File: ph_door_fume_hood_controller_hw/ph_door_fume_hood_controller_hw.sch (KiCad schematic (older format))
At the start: 249 parts, among them IC1 6N137, IC2 6N137, J1 Conn_01x03, J10 Conn_01x03, J11 Conn_01x02, J12 Conn_01x06, J13 Conn_01x02, J14 Conn_01x03, J15 Conn_01x03, J2 Conn_01x04, J3 CONN_01X04, J4 Conn_01x03, J5 Conn_01x03, J6 Conn_01x02, J7 Conn_01x06, J8 USB_OTG, J9 Conn_01x02, M1 DC-DC-24-12V-200mA, M2 MORSUN_485, Q1 C1815, Q10 A1015, Q11 Q_NMOS_GDS, Q2 Q_PMOS_GDS, Q3 Q_NMOS_GDS, Q4 Q_NMOS_GDS, Q5 C1815, Q6 Q_NMOS_GDS, Q7 Q_NMOS_GDS, Q8 C1815, Q9 Q_NMOS_GDS, U1 74HC123, U10 PC817, U11 MCP4725, U12 ASM1117-3V3, U13 PC817, U14 PC817, U15 LM358, U16 PC817, U17 PC817, U18 PC817, U19 PC817, U2 AD8601, U20 PC817, U21 PC817, U22 PC817, U23 PC817, U3 PC817, U4 PC817, U5 TB6600, U6 PC817, U7 STM32F103C8, U8 ASM1117, U9 XL4015, Y1 Crystal, Y2 32768Mhz

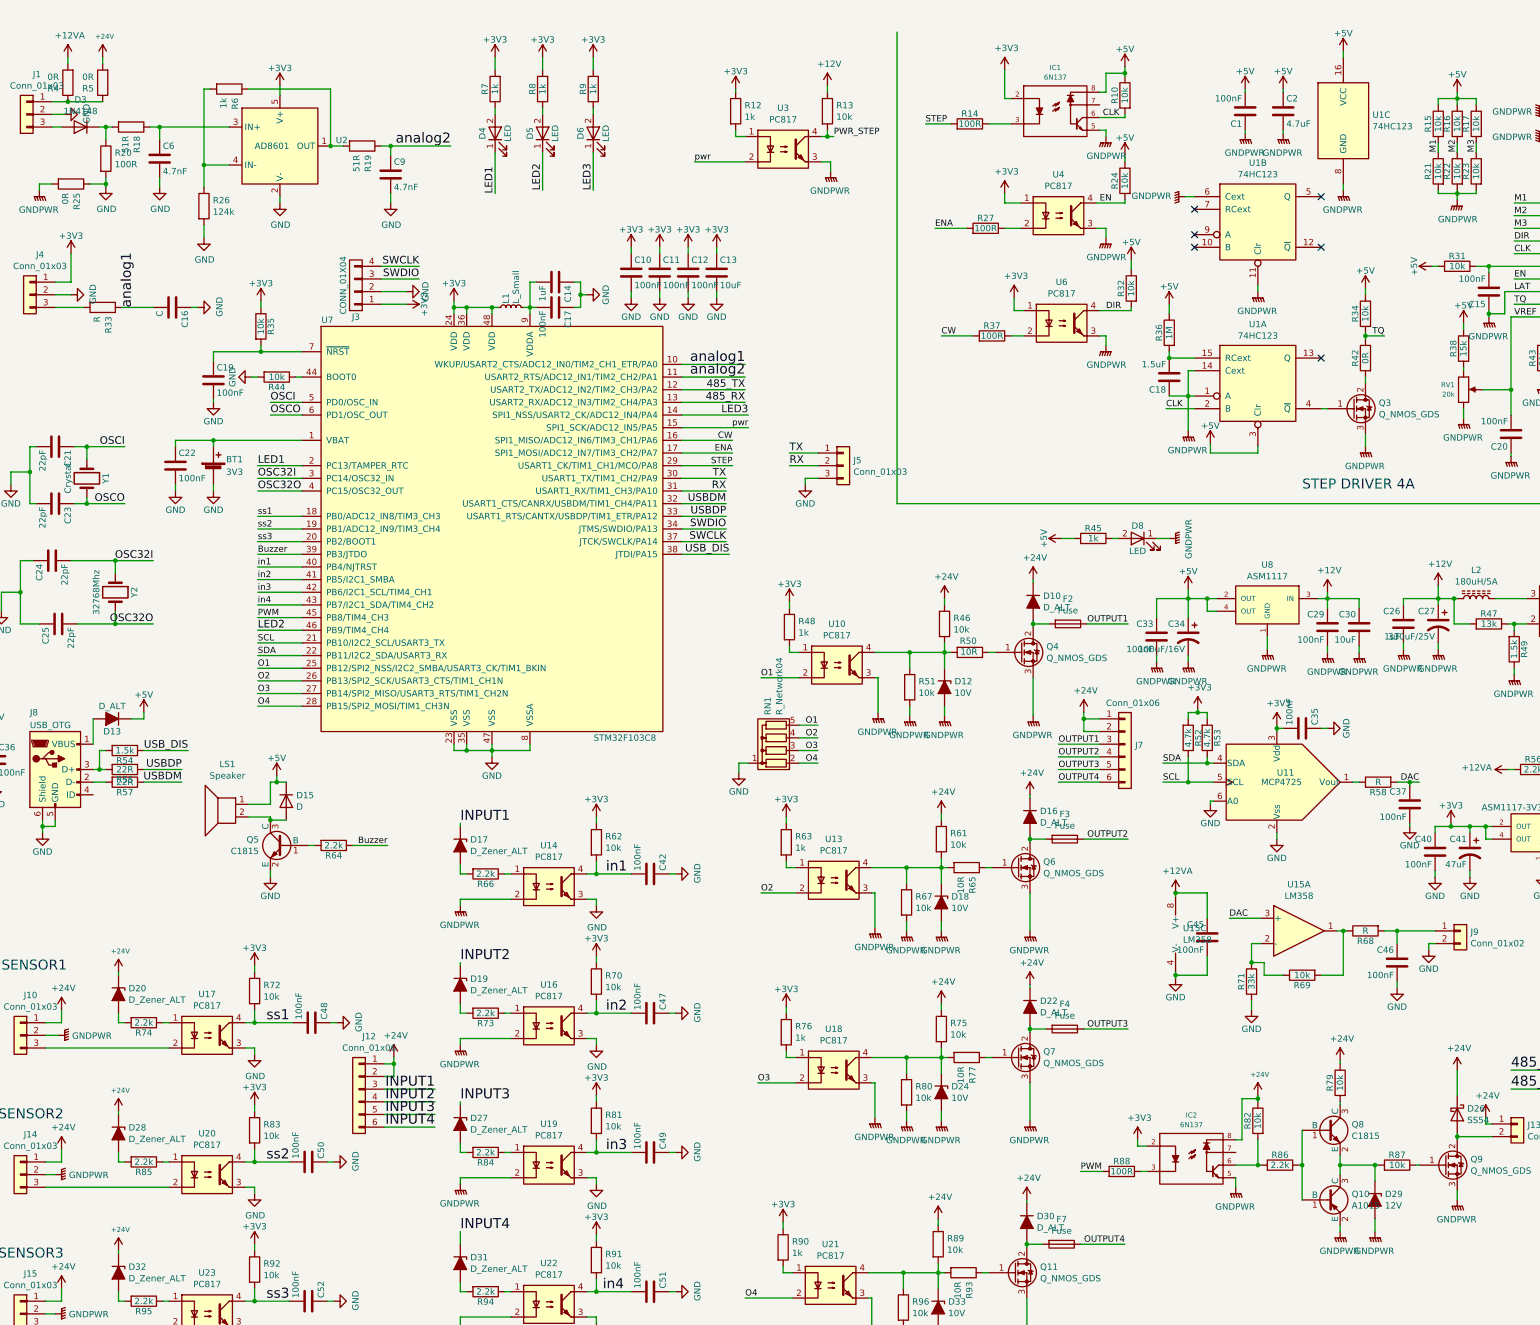
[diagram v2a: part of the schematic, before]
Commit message: Layoutting Board Door-Fume-Hood
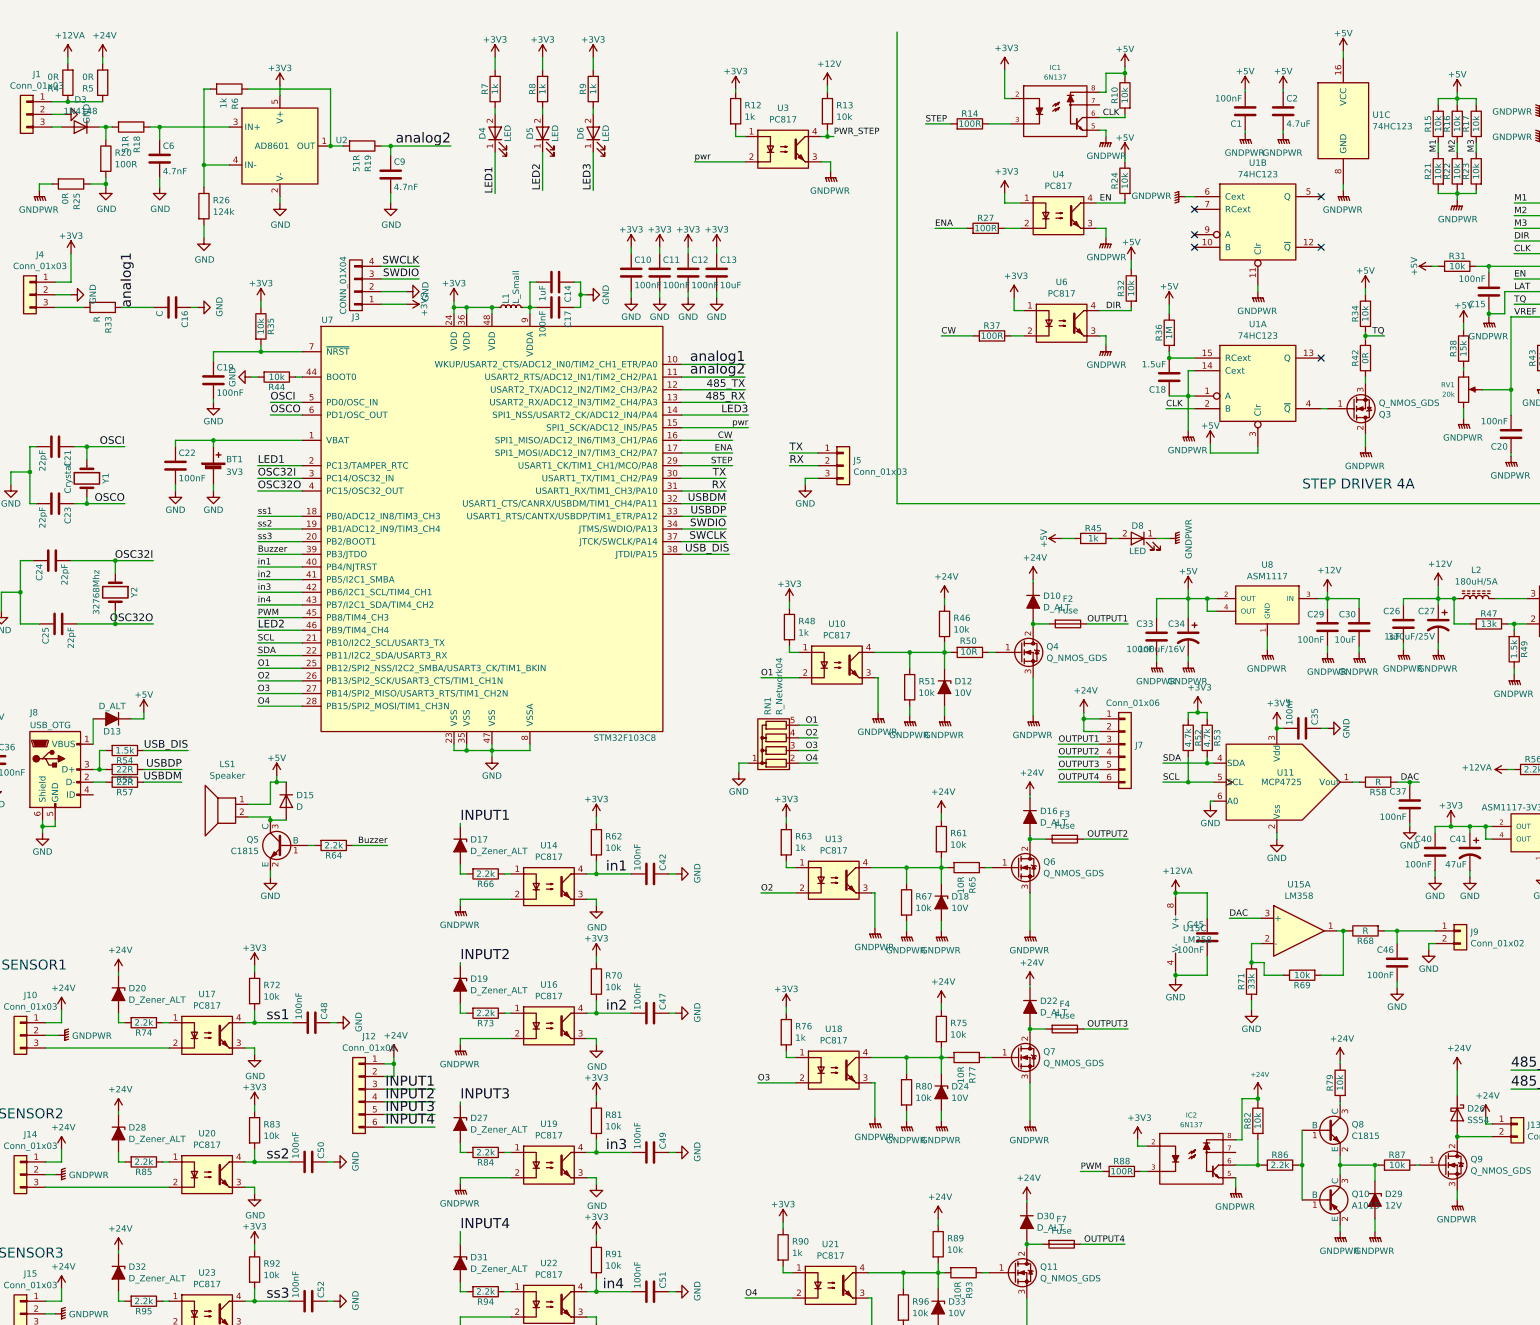
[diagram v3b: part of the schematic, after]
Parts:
- J1, J4, J5: footprint VinhTho_Lib:TerminalBlock-WAGO-3P -> Connector_PinSocket_2.54mm:PinSocket_1x03_P2.54mm_Vertical
- J10, J14, J15: footprint VinhTho_Lib:TerminalBlock-WAGO-3P -> VinhTho_Lib:TerminalBlock_WAGO_2.54mm_3P
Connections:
- net +24V: now also D20.1 (K), D28.1 (K), D32.1 (K), R5.2
- net GNDPWR: now also Q3.2 (D); no longer Q3.3 (S)
- net at R42.2: now also Q3.3 (S); no longer Q3.2 (D)
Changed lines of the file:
@@
 $EndComp
 $Comp
-L master-node-rescue:C C10
-U 1 1 595ADDFC
-P 5550 2400
-F 0 "C10" H 5575 2500 50  0000 L CNN
-F 1 "100nF" H 5575 2300 50  0000 L CNN
-F 2 "Capacitor_SMD:C_0805_2012Metric_Pad1.15x1.40mm_HandSolder" H 5588 2250 50  0001 C CNN
-F 3 "" H 5550 2400 50  0001 C CNN
-	1    5550 2400
-	1    0    0    -1
-$EndComp
-$Comp
 L master-node-rescue:+3V3 #PWR063
 U 1 1 595B16DC
@@
 F 3 "https://banlinhkien.com/30n06-fqd30n06-to252-mosfet-nch-22a-60v-p12118703.html" H 11250 3475 50  0001 C CNN
 	1    11250 3475
-	1    0    0    -1
+	1    0    0    1
 $EndComp
 Wire Wire Line
@@
 $EndComp
 $Comp
-L ph_door_fume_hood_controller_hw-rescue:+24V-PH_LIB #PWR0153
-U 1 1 5ED636E7
-P 1500 7925
-F 0 "#PWR0153" H 1500 7775 50  0001 C CNN
-F 1 "+24V" H 1515 8090 39  0000 C CNN
-F 2 "" H 1500 7925 50  0001 C CNN
-F 3 "" H 1500 7925 50  0001 C CNN
-	1    1500 7925
-	1    0    0    -1
-$EndComp
-$Comp
 L Device:D_Zener_ALT D20
 U 1 1 5ED63ED3
@@
 $EndComp
 $Comp
-L ph_door_fume_hood_controller_hw-rescue:+24V-PH_LIB #PWR0175
-U 1 1 5EEE7342
-P 1500 9025
-F 0 "#PWR0175" H 1500 8875 50  0001 C CNN
-F 1 "+24V" H 1515 9190 39  0000 C CNN
-F 2 "" H 1500 9025 50  0001 C CNN
-F 3 "" H 1500 9025 50  0001 C CNN
-	1    1500 9025
-	1    0    0    -1
-$EndComp
-$Comp
 L Device:D_Zener_ALT D28
 U 1 1 5EEE7348
@@
 	2575 9425 2850 9425
 $Comp
-L Isolator:PC817 U23
-U 1 1 5EF16235
-P 2200 10625
-F 0 "U23" H 2200 10950 50  0000 C CNN
-F 1 "PC817" H 2200 10859 50  0000 C CNN
-F 2 "Package_DIP:DIP-4_W7.62mm" H 2000 10425 50  0001 L CIN
-F 3 "http://www.soselectronic.cz/a_info/resource/d/pc817.pdf" H 2200 10625 50  0001 L CNN
-	1    2200 10625
-	1    0    0    -1
-$EndComp
-$Comp
-L ph_door_fume_hood_controller_hw-rescue:+24V-PH_LIB #PWR0198
-U 1 1 5EF1623B
-P 1500 10125
-F 0 "#PWR0198" H 1500 9975 50  0001 C CNN
-F 1 "+24V" H 1515 10290 39  0000 C CNN
-F 2 "" H 1500 10125 50  0001 C CNN
-F 3 "" H 1500 10125 50  0001 C CNN
-	1    1500 10125
-	1    0    0    -1
-$EndComp
-$Comp
 L Device:D_Zener_ALT D32
 U 1 1 5EF16241
@@
 F 0 "J4" H 720 2892 50  0000 C CNN
 F 1 "Conn_01x03" H 720 2801 50  0000 C CNN
-F 2 "VinhTho_Lib:TerminalBlock-WAGO-3P" H 800 2575 50  0001 C CNN
+F 2 "Connector_PinSocket_2.54mm:PinSocket_1x03_P2.54mm_Vertical" H 800 2575 50  0001 C CNN
 F 3 "~" H 800 2575 50  0001 C CNN
 	1    800  2575
@@
 F 0 "J10" H 645 8742 50  0000 C CNN
 F 1 "Conn_01x03" H 645 8651 50  0000 C CNN
-F 2 "VinhTho_Lib:TerminalBlock-WAGO-3P" H 725 8425 50  0001 C CNN
+F 2 "VinhTho_Lib:TerminalBlock_WAGO_2.54mm_3P" H 725 8425 50  0001 C CNN
 F 3 "~" H 725 8425 50  0001 C CNN
 	1    725  8425
@@
 F 0 "J14" H 645 9842 50  0000 C CNN
 F 1 "Conn_01x03" H 645 9751 50  0000 C CNN
-F 2 "VinhTho_Lib:TerminalBlock-WAGO-3P" H 725 9525 50  0001 C CNN
+F 2 "VinhTho_Lib:TerminalBlock_WAGO_2.54mm_3P" H 725 9525 50  0001 C CNN
 F 3 "~" H 725 9525 50  0001 C CNN
 	1    725  9525
@@
 F 0 "J15" H 645 10942 50  0000 C CNN
 F 1 "Conn_01x03" H 645 10851 50  0000 C CNN
-F 2 "VinhTho_Lib:TerminalBlock-WAGO-3P" H 725 10625 50  0001 C CNN
+F 2 "VinhTho_Lib:TerminalBlock_WAGO_2.54mm_3P" H 725 10625 50  0001 C CNN
 F 3 "~" H 725 10625 50  0001 C CNN
 	1    725  10625
@@
 F 0 "J1" H 695 1467 50  0000 C CNN
 F 1 "Conn_01x03" H 695 1376 50  0000 C CNN
-F 2 "VinhTho_Lib:TerminalBlock-WAGO-3P" H 775 1150 50  0001 C CNN
+F 2 "Connector_PinSocket_2.54mm:PinSocket_1x03_P2.54mm_Vertical" H 775 1150 50  0001 C CNN
 F 3 "~" H 775 1150 50  0001 C CNN
 	1    775  1150
@@
 Wire Wire Line
 	1100 700  1100 750
-$Comp
-L ph_door_fume_hood_controller_hw-rescue:+24V-PH_LIB #PWR04
-U 1 1 5DEE7A26
-P 1375 700
-F 0 "#PWR04" H 1375 550 50  0001 C CNN
-F 1 "+24V" H 1390 865 39  0000 C CNN
-F 2 "" H 1375 700 50  0001 C CNN
-F 3 "" H 1375 700 50  0001 C CNN
-	1    1375 700
-	1    0    0    -1
-$EndComp
 Wire Wire Line
 	5950 3525 6475 3525
@@
 F 0 "J5" H 7305 3967 50  0000 L CNN
 F 1 "Conn_01x03" H 7305 3876 50  0000 L CNN
-F 2 "VinhTho_Lib:TerminalBlock-WAGO-3P" H 7225 3925 50  0001 C CNN
+F 2 "Connector_PinSocket_2.54mm:PinSocket_1x03_P2.54mm_Vertical" H 7225 3925 50  0001 C CNN
 F 3 "~" H 7225 3925 50  0001 C CNN
 	1    7225 3925
@@
 $EndComp
 $Comp
-L power:+24V #PWR0134
-U 1 1 5E2D94A6
-P 15450 7000
-F 0 "#PWR0134" H 15450 6850 50  0001 C CNN
-F 1 "+24V" H 15465 7173 50  0000 C CNN
-F 2 "" H 15450 7000 50  0001 C CNN
-F 3 "" H 15450 7000 50  0001 C CNN
-	1    15450 7000
-	1    0    0    -1
-$EndComp
-$Comp
 L power:+24V #PWR0171
 U 1 1 5E2FE88F
@@
 $EndComp
 $Comp
-L power:+24V #PWR?
+L power:+24V #PWR0153
 U 1 1 5E724D4F
 P 1050 8225
-F 0 "#PWR?" H 1050 8075 50  0001 C CNN
+F 0 "#PWR0153" H 1050 8075 50  0001 C CNN
 F 1 "+24V" H 1065 8398 50  0000 C CNN
 F 2 "" H 1050 8225 50  0001 C CNN
@@
 $EndComp
 $Comp
-L power:+24V #PWR?
+L power:+24V #PWR0159
 U 1 1 5E725FB4
 P 1050 9325
-F 0 "#PWR?" H 1050 9175 50  0001 C CNN
+F 0 "#PWR0159" H 1050 9175 50  0001 C CNN
 F 1 "+24V" H 1065 9498 50  0000 C CNN
 F 2 "" H 1050 9325 50  0001 C CNN
@@
 $EndComp
 $Comp
-L power:+24V #PWR?
+L power:+24V #PWR0175
 U 1 1 5E7283B8
 P 1050 10425
-F 0 "#PWR?" H 1050 10275 50  0001 C CNN
+F 0 "#PWR0175" H 1050 10275 50  0001 C CNN
 F 1 "+24V" H 1065 10598 50  0000 C CNN
 F 2 "" H 1050 10425 50  0001 C CNN
@@
 	1    0    0    -1
 $EndComp
+$Comp
+L Isolator:PC817 U23
+U 1 1 5EF16235
+P 2200 10625
+F 0 "U23" H 2200 10950 50  0000 C CNN
+F 1 "PC817" H 2200 10859 50  0000 C CNN
+F 2 "Package_DIP:DIP-4_W7.62mm" H 2000 10425 50  0001 L CIN
+F 3 "http://www.soselectronic.cz/a_info/resource/d/pc817.pdf" H 2200 10625 50  0001 L CNN
+	1    2200 10625
+	1    0    0    -1
+$EndComp
+$Comp
+L power:+24V #PWR0182
+U 1 1 5DBF911F
+P 1500 7925
+F 0 "#PWR0182" H 1500 7775 50  0001 C CNN
+F 1 "+24V" H 1515 8098 50  0000 C CNN
+F 2 "" H 1500 7925 50  0001 C CNN
+F 3 "" H 1500 7925 50  0001 C CNN
+	1    1500 7925
+	1    0    0    -1
+$EndComp
+$Comp
+L power:+24V #PWR0198
+U 1 1 5DBF9B7E
+P 1500 9025
+F 0 "#PWR0198" H 1500 8875 50  0001 C CNN
+F 1 "+24V" H 1515 9198 50  0000 C CNN
+F 2 "" H 1500 9025 50  0001 C CNN
+F 3 "" H 1500 9025 50  0001 C CNN
+	1    1500 9025
+	1    0    0    -1
+$EndComp
+$Comp
+L power:+24V #PWR0199
+U 1 1 5DBFBF1F
+P 1500 10125
+F 0 "#PWR0199" H 1500 9975 50  0001 C CNN
+F 1 "+24V" H 1515 10298 50  0000 C CNN
+F 2 "" H 1500 10125 50  0001 C CNN
+F 3 "" H 1500 10125 50  0001 C CNN
+	1    1500 10125
+	1    0    0    -1
+$EndComp
+$Comp
+L power:+24V #PWR0213
+U 1 1 5DC75FC2
+P 1375 700
+F 0 "#PWR0213" H 1375 550 50  0001 C CNN
+F 1 "+24V" H 1390 873 50  0000 C CNN
+F 2 "" H 1375 700 50  0001 C CNN
+F 3 "" H 1375 700 50  0001 C CNN
+	1    1375 700
+	1    0    0    -1
+$EndComp
+$Comp
+L master-node-rescue:C C10
+U 1 1 595ADDFC
+P 5550 2400
+F 0 "C10" H 5575 2500 50  0000 L CNN
+F 1 "100nF" H 5575 2300 50  0000 L CNN
+F 2 "Capacitor_SMD:C_0805_2012Metric_Pad1.15x1.40mm_HandSolder" H 5588 2250 50  0001 C CNN
+F 3 "" H 5550 2400 50  0001 C CNN
+	1    5550 2400
+	1    0    0    -1
+$EndComp
+$Comp
+L power:+24V #PWR0134
+U 1 1 5DFD5347
+P 15450 7000
+F 0 "#PWR0134" H 15450 6850 50  0001 C CNN
+F 1 "+24V" H 15465 7173 50  0000 C CNN
+F 2 "" H 15450 7000 50  0001 C CNN
+F 3 "" H 15450 7000 50  0001 C CNN
+	1    15450 7000
+	1    0    0    -1
+$EndComp
